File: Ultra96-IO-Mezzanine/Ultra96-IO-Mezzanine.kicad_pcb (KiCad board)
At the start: 2 copper layers, 85 x 54 mm, 46 parts, among them J2 Conn_01x08_Female, P1 CONN_02X20, P2 CONN_02X30, P3 CONN_02X20, Q1 STL6P3LLH6, U2 CP2102N-A01-GQFN24, U3 TXS0108EPW, U4 STUSB4500QTR, U5 TXS0108EPW, U6 TXS0108EPW, U7 TXS0108EPW

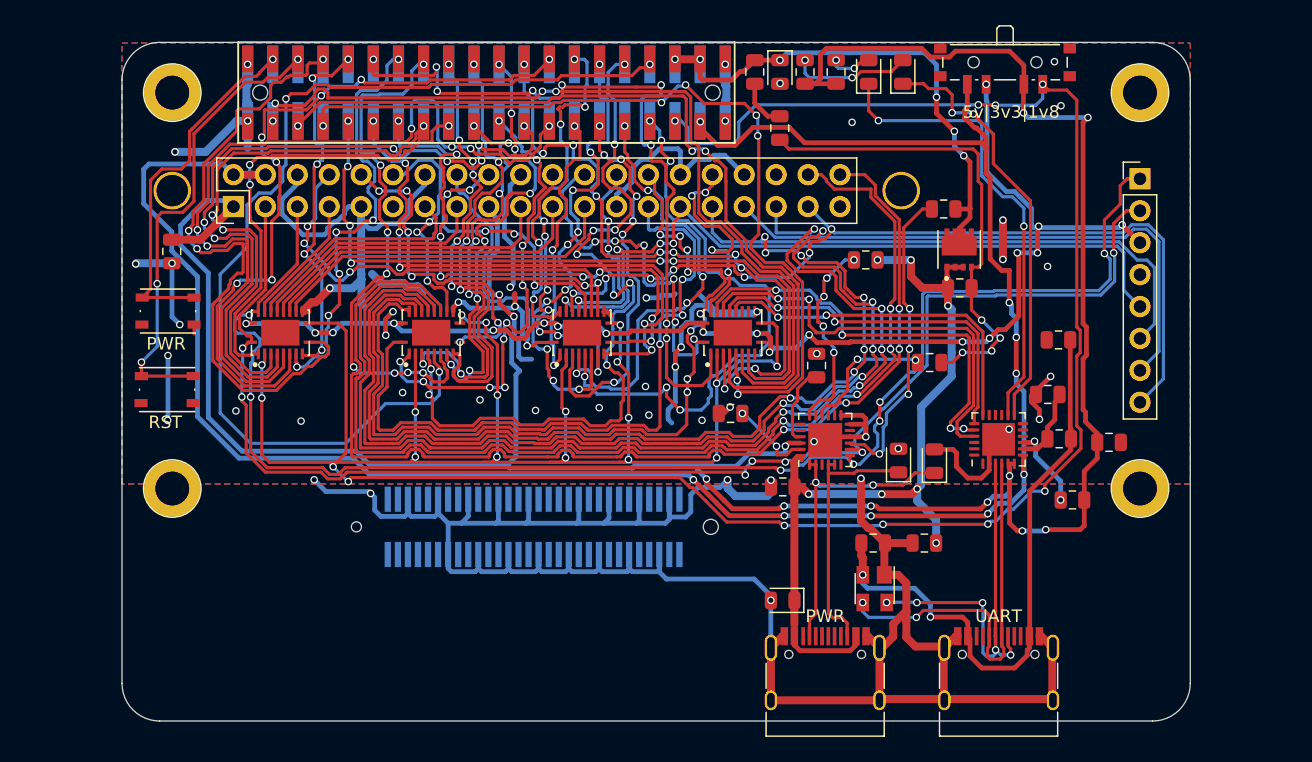
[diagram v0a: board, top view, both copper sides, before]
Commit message: Tidy up schematic
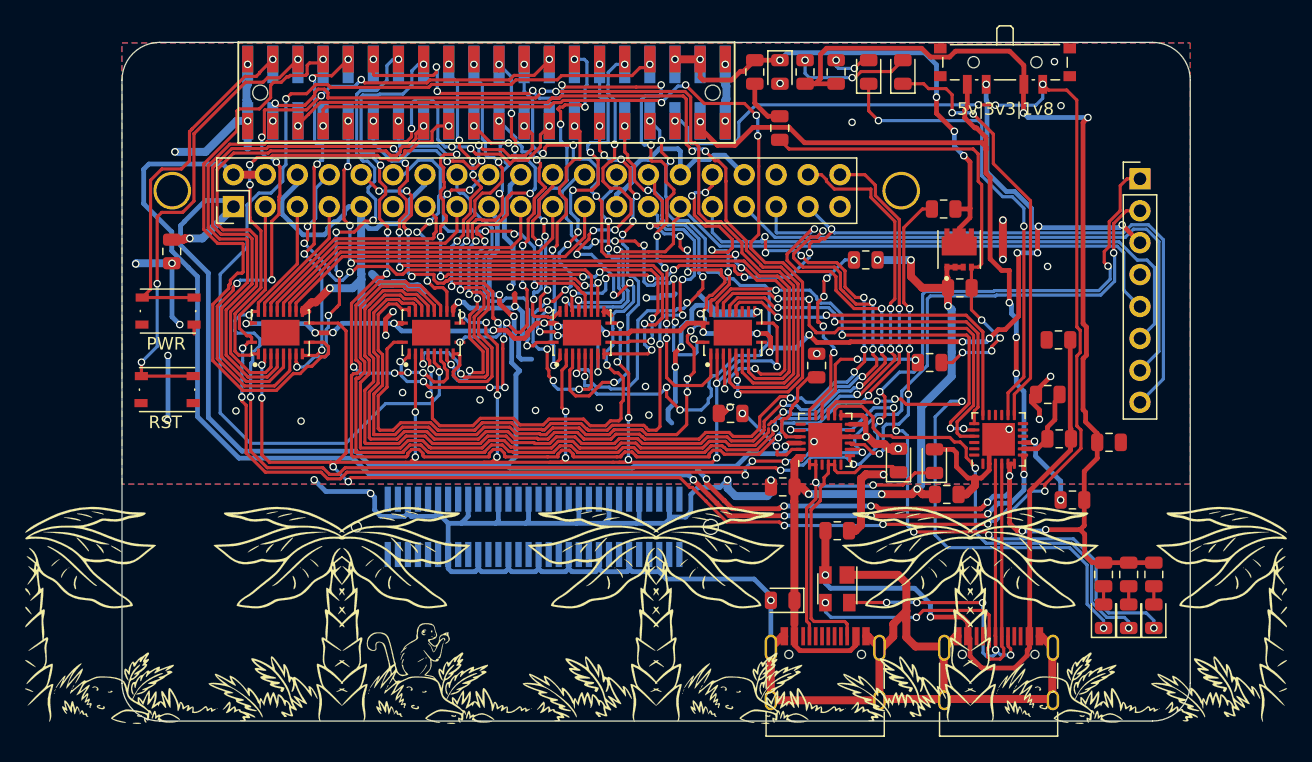
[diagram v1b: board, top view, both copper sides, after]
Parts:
- removed the REF** at (100.0, 154.0)
- added D10: LED, LED_SMD:LED_0805_2012Metric, F.Cu at (180.1, 145.7)
- added D8: LED, LED_SMD:LED_0805_2012Metric, F.Cu at (178.1, 145.7)
- added D9: LED, LED_SMD:LED_0805_2012Metric, F.Cu at (182.1, 145.7)
- added G***: LOGO, Ultra96:sloth, B.Cu at (108.0, 146.4)
- added G***: LOGO, Ultra96:no-monkey, F.Cu at (180.0, 145.5)
- added G***: LOGO, Ultra96:no-monkey, F.Cu at (155.0, 145.5)
- added G***: LOGO, Ultra96:monkey, F.Cu at (130.0, 145.5)
- added G***: LOGO, Ultra96:no-monkey, F.Cu at (105.0, 145.5)
- added R11: 1K, Resistor_SMD:R_0805_2012Metric, F.Cu at (178.1, 142.3)
- added R12: 1K, Resistor_SMD:R_0805_2012Metric, F.Cu at (182.1, 142.3)
- added R13: 1K, Resistor_SMD:R_0805_2012Metric, F.Cu at (180.1, 142.3)
- added REF**: OSHW-Symbol_8.9x8mm_SilkScreen, Symbol:OSHW-Symbol_8.9x8mm_SilkScreen, B.Cu at (179.2, 146.2)
- moved C5 4.26 mm to (165.6, 136.0), turned to 0 degrees
- moved C2 3.02 mm to (156.9, 138.9)
- moved D3 2.97 mm to (156.9, 143.5)
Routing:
- net Net-(D9-Pad1): track 0.00 -> 45.0 mm, vias 0 -> 6
- net Net-(D8-Pad1): track 0.00 -> 42.8 mm, vias 0 -> 4
- net Net-(D10-Pad1): track 0.00 -> 37.4 mm, vias 0 -> 2
- net +3V3: track 206.8 -> 215.1 mm, vias 12 -> 13
- net GND: track 343.3 -> 347.5 mm
- net VBUS: track 48.2 -> 52.1 mm
- net VBUS_PWR: track 63.8 -> 60.4 mm, vias 7 -> 6
- net D+: track 31.0 -> 34.0 mm
- net D-: track 31.5 -> 34.5 mm
- net SPIO_SCL: track 50.6 -> 47.8 mm, vias 3 -> 1
- net CC2: track 20.9 -> 23.5 mm
- net GPIO_C: track 64.7 -> 62.7 mm, vias 6 -> 4
- net Net-(C7-Pad1): track 6.68 -> 8.47 mm
- net Net-(D9-Pad2): track 0.00 -> 1.45 mm
- net Net-(D8-Pad2): track 0.00 -> 1.45 mm
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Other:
- board text added: "RevA"
- board text added: "bucknalla"

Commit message: prototyped version
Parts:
- added REF**: 96Boards CE Outline Standard, 96boards:96Boards_CE_outline_std, F.Cu at (100.0, 154.0)
- moved R9 1.24 mm to (166.6, 112.9)
- moved R11 0.40 mm to (178.1, 141.9)
- moved R12 0.40 mm to (182.1, 141.9)
- moved R13 0.40 mm to (180.1, 141.9)
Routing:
- net +5V: track 163.6 -> 156.6 mm
- net +3V3: track 215.1 -> 208.9 mm
- net Net-(D8-Pad1): track 42.8 -> 38.3 mm
- net PCM_DO_RPI: track 89.9 -> 88.3 mm
- net PCM_DI_RPI: track 89.1 -> 87.9 mm
- net Net-(R9-Pad2): track 25.3 -> 26.5 mm
- net SYS_DCIN: track 40.7 -> 39.6 mm
- net I2C1_SDA: vias 10 -> 8
